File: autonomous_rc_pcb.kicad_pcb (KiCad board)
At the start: 6 copper layers, 91.1 x 143.4 mm, 231 parts, among them J9 Micro_SD_Card, P1 USB_A_Vertical, P2 HDMI_PAUL, P7 USB_A_Vertical, U1 MCP1603L, U10 ECMF04-4HSM10, U11 CM1624, U12 ECMF04-4HSM10, U13 USB2514Bi, U14 LAN9514/LAN9514i, U15 Wurth_Magnetics_749010012A, U16 AP3512E, U2 MCP16311/2, U3 LM2576S-12/NOPB, U4 Autopilot_module, U5 ESD-8040, U6 CC2520, U7 CC2592, U8 CC112X, X1 32Mhz, X2 32MHZ, X3 XRCGB24M000F2P00R0, X4 XRCGB25M000F2P00R0

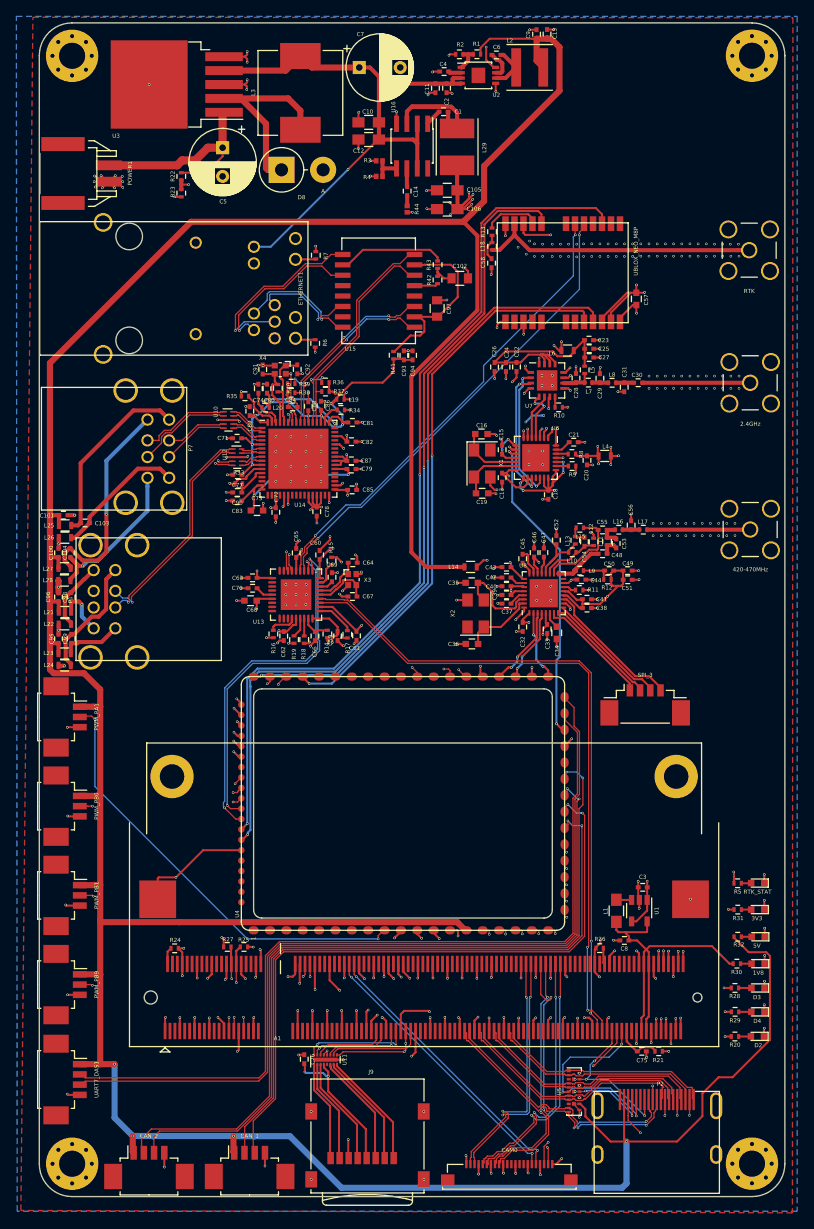
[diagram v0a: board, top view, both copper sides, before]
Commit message: tuned rf
added u.fl connectors to tune line 
moved some lines under rf components
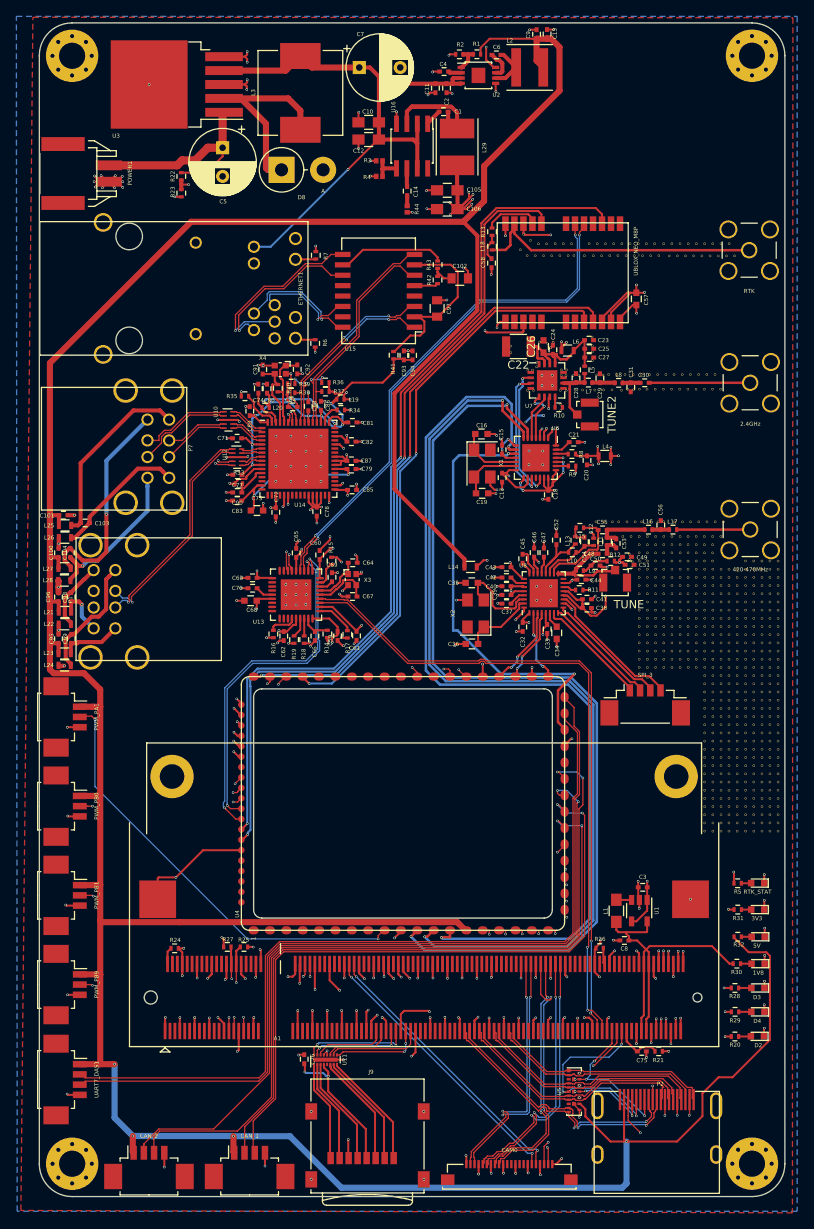
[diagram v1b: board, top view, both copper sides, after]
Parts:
- added REF**: VIA-0.3mm, Don-VIA:VIA-0.3mm, F.Cu at (154.3, 122.7)
- added REF**: VIA-0.3mm, Don-VIA:VIA-0.3mm, F.Cu at (153.3, 126.7)
- added REF**: VIA-0.3mm, Don-VIA:VIA-0.3mm, F.Cu at (155.4, 115.7)
- added REF**: VIA-0.3mm, Don-VIA:VIA-0.3mm, F.Cu at (156.4, 115.7)
- added REF**: VIA-0.3mm, Don-VIA:VIA-0.3mm, F.Cu at (156.4, 116.7)
- added REF**: VIA-0.3mm, Don-VIA:VIA-0.3mm, F.Cu at (156.4, 114.7)
- added REF**: VIA-0.3mm, Don-VIA:VIA-0.3mm, F.Cu at (158.3, 117.7)
- added REF**: VIA-0.3mm, Don-VIA:VIA-0.3mm, F.Cu at (159.3, 117.7)
- added REF**: VIA-0.3mm, Don-VIA:VIA-0.3mm, F.Cu at (159.3, 119.7)
- added REF**: VIA-0.3mm, Don-VIA:VIA-0.3mm, F.Cu at (158.3, 119.7)
- added REF**: VIA-0.3mm, Don-VIA:VIA-0.3mm, F.Cu at (158.3, 118.7)
- added REF**: VIA-0.3mm, Don-VIA:VIA-0.3mm, F.Cu at (159.3, 118.7)
- added REF**: VIA-0.3mm, Don-VIA:VIA-0.3mm, F.Cu at (152.4, 125.7)
- added REF**: VIA-0.3mm, Don-VIA:VIA-0.3mm, F.Cu at (154.3, 114.7)
- added REF**: VIA-0.3mm, Don-VIA:VIA-0.3mm, F.Cu at (154.3, 115.7)
- added REF**: VIA-0.3mm, Don-VIA:VIA-0.3mm, F.Cu at (154.3, 116.7)
- added REF**: VIA-0.3mm, Don-VIA:VIA-0.3mm, F.Cu at (155.4, 114.7)
- added REF**: VIA-0.3mm, Don-VIA:VIA-0.3mm, F.Cu at (154.3, 118.7)
- added REF**: VIA-0.3mm, Don-VIA:VIA-0.3mm, F.Cu at (154.3, 119.7)
- added REF**: VIA-0.3mm, Don-VIA:VIA-0.3mm, F.Cu at (155.4, 119.7)
- added REF**: VIA-0.3mm, Don-VIA:VIA-0.3mm, F.Cu at (155.4, 117.7)
- added REF**: VIA-0.3mm, Don-VIA:VIA-0.3mm, F.Cu at (155.4, 118.7)
- added REF**: VIA-0.3mm, Don-VIA:VIA-0.3mm, F.Cu at (154.3, 117.7)
- added REF**: VIA-0.3mm, Don-VIA:VIA-0.3mm, F.Cu at (150.4, 125.7)
- added REF**: VIA-0.3mm, Don-VIA:VIA-0.3mm, F.Cu at (157.4, 115.7)
- added REF**: VIA-0.3mm, Don-VIA:VIA-0.3mm, F.Cu at (158.3, 114.7)
- added REF**: VIA-0.3mm, Don-VIA:VIA-0.3mm, F.Cu at (157.4, 114.7)
- added REF**: VIA-0.3mm, Don-VIA:VIA-0.3mm, F.Cu at (159.3, 114.7)
- added REF**: VIA-0.3mm, Don-VIA:VIA-0.3mm, F.Cu at (158.3, 115.7)
- added REF**: VIA-0.3mm, Don-VIA:VIA-0.3mm, F.Cu at (157.4, 117.7)
- added REF**: VIA-0.3mm, Don-VIA:VIA-0.3mm, F.Cu at (156.4, 118.7)
- added REF**: VIA-0.3mm, Don-VIA:VIA-0.3mm, F.Cu at (157.4, 118.7)
- added REF**: VIA-0.3mm, Don-VIA:VIA-0.3mm, F.Cu at (157.4, 119.7)
- added REF**: VIA-0.3mm, Don-VIA:VIA-0.3mm, F.Cu at (156.4, 119.7)
- added REF**: VIA-0.3mm, Don-VIA:VIA-0.3mm, F.Cu at (151.4, 125.7)
- added REF**: VIA-0.3mm, Don-VIA:VIA-0.3mm, F.Cu at (156.4, 117.7)
- added REF**: VIA-0.3mm, Don-VIA:VIA-0.3mm, F.Cu at (152.4, 108.7)
- added REF**: VIA-0.3mm, Don-VIA:VIA-0.3mm, F.Cu at (153.3, 108.7)
- added REF**: VIA-0.3mm, Don-VIA:VIA-0.3mm, F.Cu at (152.4, 109.7)
- added REF**: VIA-0.3mm, Don-VIA:VIA-0.3mm, F.Cu at (154.3, 108.7)
- added REF**: VIA-0.3mm, Don-VIA:VIA-0.3mm, F.Cu at (153.3, 109.7)
- added REF**: VIA-0.3mm, Don-VIA:VIA-0.3mm, F.Cu at (154.3, 109.7)
- added REF**: VIA-0.3mm, Don-VIA:VIA-0.3mm, F.Cu at (154.3, 113.7)
- added REF**: VIA-0.3mm, Don-VIA:VIA-0.3mm, F.Cu at (153.3, 113.7)
- added REF**: VIA-0.3mm, Don-VIA:VIA-0.3mm, F.Cu at (153.3, 112.7)
- added REF**: VIA-0.3mm, Don-VIA:VIA-0.3mm, F.Cu at (151.4, 126.7)
- added REF**: VIA-0.3mm, Don-VIA:VIA-0.3mm, F.Cu at (152.4, 113.7)
- added REF**: VIA-0.3mm, Don-VIA:VIA-0.3mm, F.Cu at (154.3, 111.7)
- added REF**: VIA-0.3mm, Don-VIA:VIA-0.3mm, F.Cu at (154.3, 112.7)
- added REF**: VIA-0.3mm, Don-VIA:VIA-0.3mm, F.Cu at (152.4, 112.7)
- added REF**: VIA-0.3mm, Don-VIA:VIA-0.3mm, F.Cu at (154.3, 110.7)
- added REF**: VIA-0.3mm, Don-VIA:VIA-0.3mm, F.Cu at (151.4, 113.7)
- added REF**: VIA-0.3mm, Don-VIA:VIA-0.3mm, F.Cu at (150.4, 113.7)
- added REF**: VIA-0.3mm, Don-VIA:VIA-0.3mm, F.Cu at (150.4, 112.7)
- added REF**: VIA-0.3mm, Don-VIA:VIA-0.3mm, F.Cu at (151.4, 112.7)
- added REF**: VIA-0.3mm, Don-VIA:VIA-0.3mm, F.Cu at (150.4, 111.7)
- added REF**: VIA-0.3mm, Don-VIA:VIA-0.3mm, F.Cu at (150.4, 126.7)
- added REF**: VIA-0.3mm, Don-VIA:VIA-0.3mm, F.Cu at (150.4, 110.7)
- added REF**: VIA-0.3mm, Don-VIA:VIA-0.3mm, F.Cu at (151.4, 111.7)
- added REF**: VIA-0.3mm, Don-VIA:VIA-0.3mm, F.Cu at (151.4, 110.7)
- added REF**: VIA-0.3mm, Don-VIA:VIA-0.3mm, F.Cu at (151.4, 107.7)
- added REF**: VIA-0.3mm, Don-VIA:VIA-0.3mm, F.Cu at (150.4, 107.7)
- added REF**: VIA-0.3mm, Don-VIA:VIA-0.3mm, F.Cu at (153.3, 107.7)
- added REF**: VIA-0.3mm, Don-VIA:VIA-0.3mm, F.Cu at (152.4, 107.7)
- added REF**: VIA-0.3mm, Don-VIA:VIA-0.3mm, F.Cu at (154.3, 107.7)
- added REF**: VIA-0.3mm, Don-VIA:VIA-0.3mm, F.Cu at (157.4, 113.7)
- added REF**: VIA-0.3mm, Don-VIA:VIA-0.3mm, F.Cu at (155.4, 111.7)
- added REF**: VIA-0.3mm, Don-VIA:VIA-0.3mm, F.Cu at (150.4, 123.7)
- added REF**: VIA-0.3mm, Don-VIA:VIA-0.3mm, F.Cu at (155.4, 112.7)
- added REF**: VIA-0.3mm, Don-VIA:VIA-0.3mm, F.Cu at (155.4, 113.7)
- added REF**: VIA-0.3mm, Don-VIA:VIA-0.3mm, F.Cu at (156.4, 113.7)
- added REF**: VIA-0.3mm, Don-VIA:VIA-0.3mm, F.Cu at (159.3, 113.7)
- added REF**: VIA-0.3mm, Don-VIA:VIA-0.3mm, F.Cu at (158.3, 111.7)
- added REF**: VIA-0.3mm, Don-VIA:VIA-0.3mm, F.Cu at (159.3, 112.7)
- added REF**: VIA-0.3mm, Don-VIA:VIA-0.3mm, F.Cu at (159.3, 111.7)
- added REF**: VIA-0.3mm, Don-VIA:VIA-0.3mm, F.Cu at (158.3, 112.7)
- added REF**: VIA-0.3mm, Don-VIA:VIA-0.3mm, F.Cu at (158.3, 113.7)
- added REF**: VIA-0.3mm, Don-VIA:VIA-0.3mm, F.Cu at (157.4, 112.7)
- added REF**: VIA-0.3mm, Don-VIA:VIA-0.3mm, F.Cu at (150.4, 122.7)
- added REF**: VIA-0.3mm, Don-VIA:VIA-0.3mm, F.Cu at (156.4, 111.7)
- added REF**: VIA-0.3mm, Don-VIA:VIA-0.3mm, F.Cu at (157.4, 111.7)
- added REF**: VIA-0.3mm, Don-VIA:VIA-0.3mm, F.Cu at (156.4, 112.7)
- added REF**: VIA-0.3mm, Don-VIA:VIA-0.3mm, F.Cu at (155.4, 109.7)
- added REF**: VIA-0.3mm, Don-VIA:VIA-0.3mm, F.Cu at (156.4, 110.7)
- added REF**: VIA-0.3mm, Don-VIA:VIA-0.3mm, F.Cu at (155.4, 110.7)
- added REF**: VIA-0.3mm, Don-VIA:VIA-0.3mm, F.Cu at (156.4, 109.7)
- added REF**: VIA-0.3mm, Don-VIA:VIA-0.3mm, F.Cu at (159.3, 109.7)
- added REF**: VIA-0.3mm, Don-VIA:VIA-0.3mm, F.Cu at (158.3, 109.7)
- added REF**: VIA-0.3mm, Don-VIA:VIA-0.3mm, F.Cu at (157.4, 109.7)
- added REF**: VIA-0.3mm, Don-VIA:VIA-0.3mm, F.Cu at (151.4, 123.7)
- added REF**: VIA-0.3mm, Don-VIA:VIA-0.3mm, F.Cu at (158.3, 110.7)
- added REF**: VIA-0.3mm, Don-VIA:VIA-0.3mm, F.Cu at (159.3, 110.7)
- added REF**: VIA-0.3mm, Don-VIA:VIA-0.3mm, F.Cu at (157.4, 110.7)
- added REF**: VIA-0.3mm, Don-VIA:VIA-0.3mm, F.Cu at (156.4, 107.7)
- added REF**: VIA-0.3mm, Don-VIA:VIA-0.3mm, F.Cu at (155.4, 108.7)
- added REF**: VIA-0.3mm, Don-VIA:VIA-0.3mm, F.Cu at (155.4, 107.7)
- added REF**: VIA-0.3mm, Don-VIA:VIA-0.3mm, F.Cu at (156.4, 108.7)
- added REF**: VIA-0.3mm, Don-VIA:VIA-0.3mm, F.Cu at (159.3, 107.7)
- added REF**: VIA-0.3mm, Don-VIA:VIA-0.3mm, F.Cu at (158.3, 108.7)
- added REF**: VIA-0.3mm, Don-VIA:VIA-0.3mm, F.Cu at (157.4, 107.7)
- added REF**: VIA-0.3mm, Don-VIA:VIA-0.3mm, F.Cu at (151.4, 122.7)
- added REF**: VIA-0.3mm, Don-VIA:VIA-0.3mm, F.Cu at (158.3, 107.7)
- added REF**: VIA-0.3mm, Don-VIA:VIA-0.3mm, F.Cu at (159.3, 108.7)
- added REF**: VIA-0.3mm, Don-VIA:VIA-0.3mm, F.Cu at (157.4, 108.7)
- added REF**: VIA-0.3mm, Don-VIA:VIA-0.3mm, F.Cu at (152.4, 110.7)
- added REF**: VIA-0.3mm, Don-VIA:VIA-0.3mm, F.Cu at (153.3, 111.7)
- added REF**: VIA-0.3mm, Don-VIA:VIA-0.3mm, F.Cu at (152.4, 111.7)
- added REF**: VIA-0.3mm, Don-VIA:VIA-0.3mm, F.Cu at (153.3, 110.7)
- added REF**: VIA-0.3mm, Don-VIA:VIA-0.3mm, F.Cu at (151.4, 108.7)
- added REF**: VIA-0.3mm, Don-VIA:VIA-0.3mm, F.Cu at (151.4, 109.7)
- added REF**: VIA-0.3mm, Don-VIA:VIA-0.3mm, F.Cu at (150.4, 109.7)
- added REF**: VIA-0.3mm, Don-VIA:VIA-0.3mm, F.Cu at (154.3, 121.7)
- added REF**: VIA-0.3mm, Don-VIA:VIA-0.3mm, F.Cu at (150.4, 124.7)
- added REF**: VIA-0.3mm, Don-VIA:VIA-0.3mm, F.Cu at (150.4, 108.7)
- added REF**: VIA-0.3mm, Don-VIA:VIA-0.3mm, F.Cu at (142.4, 102.7)
- added REF**: VIA-0.3mm, Don-VIA:VIA-0.3mm, F.Cu at (143.4, 102.7)
- added REF**: VIA-0.3mm, Don-VIA:VIA-0.3mm, F.Cu at (144.4, 102.7)
- added REF**: VIA-0.3mm, Don-VIA:VIA-0.3mm, F.Cu at (145.4, 103.7)
- added REF**: VIA-0.3mm, Don-VIA:VIA-0.3mm, F.Cu at (145.4, 102.7)
- added REF**: VIA-0.3mm, Don-VIA:VIA-0.3mm, F.Cu at (144.4, 103.7)
- added REF**: VIA-0.3mm, Don-VIA:VIA-0.3mm, F.Cu at (143.4, 103.7)
- added REF**: VIA-0.3mm, Don-VIA:VIA-0.3mm, F.Cu at (142.4, 104.7)
- added REF**: VIA-0.3mm, Don-VIA:VIA-0.3mm, F.Cu at (143.4, 104.7)
- added REF**: VIA-0.3mm, Don-VIA:VIA-0.3mm, F.Cu at (151.4, 124.7)
- added REF**: VIA-0.3mm, Don-VIA:VIA-0.3mm, F.Cu at (143.4, 105.7)
- added REF**: VIA-0.3mm, Don-VIA:VIA-0.3mm, F.Cu at (143.4, 106.7)
- added REF**: VIA-0.3mm, Don-VIA:VIA-0.3mm, F.Cu at (142.4, 106.7)
- added REF**: VIA-0.3mm, Don-VIA:VIA-0.3mm, F.Cu at (142.4, 103.7)
- added REF**: VIA-0.3mm, Don-VIA:VIA-0.3mm, F.Cu at (142.4, 105.7)
- added REF**: VIA-0.3mm, Don-VIA:VIA-0.3mm, F.Cu at (148.3, 104.7)
- added REF**: VIA-0.3mm, Don-VIA:VIA-0.3mm, F.Cu at (149.3, 103.7)
- added REF**: VIA-0.3mm, Don-VIA:VIA-0.3mm, F.Cu at (148.3, 103.7)
- added REF**: VIA-0.3mm, Don-VIA:VIA-0.3mm, F.Cu at (147.4, 103.7)
- added REF**: VIA-0.3mm, Don-VIA:VIA-0.3mm, F.Cu at (146.4, 103.7)
- added REF**: VIA-0.3mm, Don-VIA:VIA-0.3mm, F.Cu at (154.3, 124.7)
- added REF**: VIA-0.3mm, Don-VIA:VIA-0.3mm, F.Cu at (147.4, 104.7)
- added REF**: VIA-0.3mm, Don-VIA:VIA-0.3mm, F.Cu at (146.4, 104.7)
- added REF**: VIA-0.3mm, Don-VIA:VIA-0.3mm, F.Cu at (147.4, 105.7)
- added REF**: VIA-0.3mm, Don-VIA:VIA-0.3mm, F.Cu at (146.4, 105.7)
- added REF**: VIA-0.3mm, Don-VIA:VIA-0.3mm, F.Cu at (144.4, 106.7)
- added REF**: VIA-0.3mm, Don-VIA:VIA-0.3mm, F.Cu at (144.4, 105.7)
- added REF**: VIA-0.3mm, Don-VIA:VIA-0.3mm, F.Cu at (145.4, 105.7)
- added REF**: VIA-0.3mm, Don-VIA:VIA-0.3mm, F.Cu at (145.4, 106.7)
- added REF**: VIA-0.3mm, Don-VIA:VIA-0.3mm, F.Cu at (146.4, 106.7)
- added REF**: VIA-0.3mm, Don-VIA:VIA-0.3mm, F.Cu at (145.4, 104.7)
- added REF**: VIA-0.3mm, Don-VIA:VIA-0.3mm, F.Cu at (153.3, 123.7)
- added REF**: VIA-0.3mm, Don-VIA:VIA-0.3mm, F.Cu at (144.4, 104.7)
- added REF**: VIA-0.3mm, Don-VIA:VIA-0.3mm, F.Cu at (147.4, 106.7)
- added REF**: VIA-0.3mm, Don-VIA:VIA-0.3mm, F.Cu at (149.3, 105.7)
- added REF**: VIA-0.3mm, Don-VIA:VIA-0.3mm, F.Cu at (149.3, 106.7)
- added REF**: VIA-0.3mm, Don-VIA:VIA-0.3mm, F.Cu at (148.4, 105.7)
- added REF**: VIA-0.3mm, Don-VIA:VIA-0.3mm, F.Cu at (148.4, 106.7)
- added REF**: VIA-0.3mm, Don-VIA:VIA-0.3mm, F.Cu at (149.3, 104.7)
- added REF**: VIA-0.3mm, Don-VIA:VIA-0.3mm, F.Cu at (146.4, 102.7)
- added REF**: VIA-0.3mm, Don-VIA:VIA-0.3mm, F.Cu at (147.4, 102.7)
- added REF**: VIA-0.3mm, Don-VIA:VIA-0.3mm, F.Cu at (148.3, 101.7)
- added REF**: VIA-0.3mm, Don-VIA:VIA-0.3mm, F.Cu at (153.3, 125.7)
- added REF**: VIA-0.3mm, Don-VIA:VIA-0.3mm, F.Cu at (148.3, 102.7)
- added REF**: VIA-0.3mm, Don-VIA:VIA-0.3mm, F.Cu at (149.3, 101.7)
- added REF**: VIA-0.3mm, Don-VIA:VIA-0.3mm, F.Cu at (149.3, 102.7)
- added REF**: VIA-0.3mm, Don-VIA:VIA-0.3mm, F.Cu at (159.3, 106.7)
- added REF**: VIA-0.3mm, Don-VIA:VIA-0.3mm, F.Cu at (158.3, 106.7)
- added REF**: VIA-0.3mm, Don-VIA:VIA-0.3mm, F.Cu at (158.3, 105.7)
- added REF**: VIA-0.3mm, Don-VIA:VIA-0.3mm, F.Cu at (159.3, 105.7)
- added REF**: VIA-0.3mm, Don-VIA:VIA-0.3mm, F.Cu at (159.3, 104.7)
- added REF**: VIA-0.3mm, Don-VIA:VIA-0.3mm, F.Cu at (157.4, 106.7)
- added REF**: VIA-0.3mm, Don-VIA:VIA-0.3mm, F.Cu at (156.4, 106.7)
- added REF**: VIA-0.3mm, Don-VIA:VIA-0.3mm, F.Cu at (153.3, 124.7)
- added REF**: VIA-0.3mm, Don-VIA:VIA-0.3mm, F.Cu at (155.4, 105.7)
- added REF**: VIA-0.3mm, Don-VIA:VIA-0.3mm, F.Cu at (155.4, 106.7)
- added REF**: VIA-0.3mm, Don-VIA:VIA-0.3mm, F.Cu at (158.3, 104.7)
- added REF**: VIA-0.3mm, Don-VIA:VIA-0.3mm, F.Cu at (156.4, 105.7)
- added REF**: VIA-0.3mm, Don-VIA:VIA-0.3mm, F.Cu at (156.4, 104.7)
- added REF**: VIA-0.3mm, Don-VIA:VIA-0.3mm, F.Cu at (157.4, 105.7)
- added REF**: VIA-0.3mm, Don-VIA:VIA-0.3mm, F.Cu at (157.4, 104.7)
- added REF**: VIA-0.3mm, Don-VIA:VIA-0.3mm, F.Cu at (156.4, 101.7)
- added REF**: VIA-0.3mm, Don-VIA:VIA-0.3mm, F.Cu at (155.4, 101.7)
- added REF**: VIA-0.3mm, Don-VIA:VIA-0.3mm, F.Cu at (158.3, 101.7)
- added REF**: VIA-0.3mm, Don-VIA:VIA-0.3mm, F.Cu at (152.4, 123.7)
- added REF**: VIA-0.3mm, Don-VIA:VIA-0.3mm, F.Cu at (157.4, 101.7)
- added REF**: VIA-0.3mm, Don-VIA:VIA-0.3mm, F.Cu at (159.3, 101.7)
- added REF**: VIA-0.3mm, Don-VIA:VIA-0.3mm, F.Cu at (155.4, 104.7)
- added REF**: VIA-0.3mm, Don-VIA:VIA-0.3mm, F.Cu at (155.4, 103.7)
- added REF**: VIA-0.3mm, Don-VIA:VIA-0.3mm, F.Cu at (156.4, 102.7)
- added REF**: VIA-0.3mm, Don-VIA:VIA-0.3mm, F.Cu at (155.4, 102.7)
- added REF**: VIA-0.3mm, Don-VIA:VIA-0.3mm, F.Cu at (156.4, 103.7)
- added REF**: VIA-0.3mm, Don-VIA:VIA-0.3mm, F.Cu at (158.3, 103.7)
- added REF**: VIA-0.3mm, Don-VIA:VIA-0.3mm, F.Cu at (158.3, 102.7)
- added REF**: VIA-0.3mm, Don-VIA:VIA-0.3mm, F.Cu at (157.4, 103.7)
- added REF**: VIA-0.3mm, Don-VIA:VIA-0.3mm, F.Cu at (154.3, 123.7)
- added REF**: VIA-0.3mm, Don-VIA:VIA-0.3mm, F.Cu at (157.4, 102.7)
- added REF**: VIA-0.3mm, Don-VIA:VIA-0.3mm, F.Cu at (159.3, 102.7)
- added REF**: VIA-0.3mm, Don-VIA:VIA-0.3mm, F.Cu at (159.3, 103.7)
- added REF**: VIA-0.3mm, Don-VIA:VIA-0.3mm, F.Cu at (152.4, 104.7)
- added REF**: VIA-0.3mm, Don-VIA:VIA-0.3mm, F.Cu at (152.4, 103.7)
- added REF**: VIA-0.3mm, Don-VIA:VIA-0.3mm, F.Cu at (153.3, 103.7)
- added REF**: VIA-0.3mm, Don-VIA:VIA-0.3mm, F.Cu at (154.3, 104.7)
- added REF**: VIA-0.3mm, Don-VIA:VIA-0.3mm, F.Cu at (154.3, 102.7)
- added REF**: VIA-0.3mm, Don-VIA:VIA-0.3mm, F.Cu at (154.3, 103.7)
- added REF**: VIA-0.3mm, Don-VIA:VIA-0.3mm, F.Cu at (153.3, 104.7)
- added REF**: VIA-0.3mm, Don-VIA:VIA-0.3mm, F.Cu at (152.4, 124.7)
- added REF**: VIA-0.3mm, Don-VIA:VIA-0.3mm, F.Cu at (150.4, 101.7)
- added REF**: VIA-0.3mm, Don-VIA:VIA-0.3mm, F.Cu at (151.4, 102.7)
- added REF**: VIA-0.3mm, Don-VIA:VIA-0.3mm, F.Cu at (150.4, 103.7)
- added REF**: VIA-0.3mm, Don-VIA:VIA-0.3mm, F.Cu at (150.4, 102.7)
- added REF**: VIA-0.3mm, Don-VIA:VIA-0.3mm, F.Cu at (151.4, 103.7)
- added REF**: VIA-0.3mm, Don-VIA:VIA-0.3mm, F.Cu at (151.4, 101.7)
- added REF**: VIA-0.3mm, Don-VIA:VIA-0.3mm, F.Cu at (153.3, 101.7)
- added REF**: VIA-0.3mm, Don-VIA:VIA-0.3mm, F.Cu at (152.4, 102.7)
- added REF**: VIA-0.3mm, Don-VIA:VIA-0.3mm, F.Cu at (154.3, 101.7)
- added REF**: VIA-0.3mm, Don-VIA:VIA-0.3mm, F.Cu at (152.4, 101.7)
- added REF**: VIA-0.3mm, Don-VIA:VIA-0.3mm, F.Cu at (153.3, 120.7)
- added REF**: VIA-0.3mm, Don-VIA:VIA-0.3mm, F.Cu at (153.3, 102.7)
- added REF**: VIA-0.3mm, Don-VIA:VIA-0.3mm, F.Cu at (150.4, 104.7)
- added REF**: VIA-0.3mm, Don-VIA:VIA-0.3mm, F.Cu at (150.4, 106.7)
- added REF**: VIA-0.3mm, Don-VIA:VIA-0.3mm, F.Cu at (151.4, 105.7)
- added REF**: VIA-0.3mm, Don-VIA:VIA-0.3mm, F.Cu at (151.4, 104.7)
- added REF**: VIA-0.3mm, Don-VIA:VIA-0.3mm, F.Cu at (150.4, 105.7)
- added REF**: VIA-0.3mm, Don-VIA:VIA-0.3mm, F.Cu at (151.4, 106.7)
- added REF**: VIA-0.3mm, Don-VIA:VIA-0.3mm, F.Cu at (154.3, 106.7)
- added REF**: VIA-0.3mm, Don-VIA:VIA-0.3mm, F.Cu at (154.3, 105.7)
- added REF**: VIA-0.3mm, Don-VIA:VIA-0.3mm, F.Cu at (153.3, 105.7)
- added REF**: VIA-0.3mm, Don-VIA:VIA-0.3mm, F.Cu at (153.3, 122.7)
- added REF**: VIA-0.3mm, Don-VIA:VIA-0.3mm, F.Cu at (152.4, 120.7)
- added REF**: VIA-0.3mm, Don-VIA:VIA-0.3mm, F.Cu at (153.3, 106.7)
- added REF**: VIA-0.3mm, Don-VIA:VIA-0.3mm, F.Cu at (152.4, 106.7)
- added REF**: VIA-0.3mm, Don-VIA:VIA-0.3mm, F.Cu at (152.4, 105.7)
- added REF**: VIA-0.3mm, Don-VIA:VIA-0.3mm, F.Cu at (147.4, 101.7)
- added REF**: VIA-0.3mm, Don-VIA:VIA-0.3mm, F.Cu at (146.4, 101.7)
- added REF**: VIA-0.3mm, Don-VIA:VIA-0.3mm, F.Cu at (144.4, 101.7)
- added REF**: VIA-0.3mm, Don-VIA:VIA-0.3mm, F.Cu at (145.4, 101.7)
- added REF**: VIA-0.3mm, Don-VIA:VIA-0.3mm, F.Cu at (143.4, 101.7)
- added REF**: VIA-0.3mm, Don-VIA:VIA-0.3mm, F.Cu at (142.4, 101.7)
- added REF**: VIA-0.3mm, Don-VIA:VIA-0.3mm, F.Cu at (144.4, 97.7)
- added REF**: VIA-0.3mm, Don-VIA:VIA-0.3mm, F.Cu at (154.3, 120.7)
- added REF**: VIA-0.3mm, Don-VIA:VIA-0.3mm, F.Cu at (142.4, 99.7)
- added REF**: VIA-0.3mm, Don-VIA:VIA-0.3mm, F.Cu at (142.4, 100.7)
- added REF**: VIA-0.3mm, Don-VIA:VIA-0.3mm, F.Cu at (143.4, 100.7)
- added REF**: VIA-0.3mm, Don-VIA:VIA-0.3mm, F.Cu at (143.4, 99.7)
- added REF**: VIA-0.3mm, Don-VIA:VIA-0.3mm, F.Cu at (144.4, 98.7)
- added REF**: VIA-0.3mm, Don-VIA:VIA-0.3mm, F.Cu at (143.4, 98.7)
- added REF**: VIA-0.3mm, Don-VIA:VIA-0.3mm, F.Cu at (144.4, 99.7)
- added REF**: VIA-0.3mm, Don-VIA:VIA-0.3mm, F.Cu at (142.4, 98.7)
- added REF**: VIA-0.3mm, Don-VIA:VIA-0.3mm, F.Cu at (143.4, 96.7)
- added REF**: VIA-0.3mm, Don-VIA:VIA-0.3mm, F.Cu at (142.4, 97.7)
- added REF**: VIA-0.3mm, Don-VIA:VIA-0.3mm, F.Cu at (150.4, 121.7)
- added REF**: VIA-0.3mm, Don-VIA:VIA-0.3mm, F.Cu at (142.4, 96.7)
- added REF**: VIA-0.3mm, Don-VIA:VIA-0.3mm, F.Cu at (143.4, 97.7)
- added REF**: VIA-0.3mm, Don-VIA:VIA-0.3mm, F.Cu at (144.4, 100.7)
- added REF**: VIA-0.3mm, Don-VIA:VIA-0.3mm, F.Cu at (144.4, 96.7)
- added REF**: VIA-0.3mm, Don-VIA:VIA-0.3mm, F.Cu at (144.4, 95.7)
- added REF**: VIA-0.3mm, Don-VIA:VIA-0.3mm, F.Cu at (144.4, 93.7)
- added REF**: VIA-0.3mm, Don-VIA:VIA-0.3mm, F.Cu at (144.4, 94.7)
- added REF**: VIA-0.3mm, Don-VIA:VIA-0.3mm, F.Cu at (144.4, 92.7)
- added REF**: VIA-0.3mm, Don-VIA:VIA-0.3mm, F.Cu at (144.4, 91.7)
- added REF**: VIA-0.3mm, Don-VIA:VIA-0.3mm, F.Cu at (143.4, 93.7)
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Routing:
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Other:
- rule pad_to_mask_clearance: 0.2 -> 0.1

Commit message: stitched pcb, tuned rf
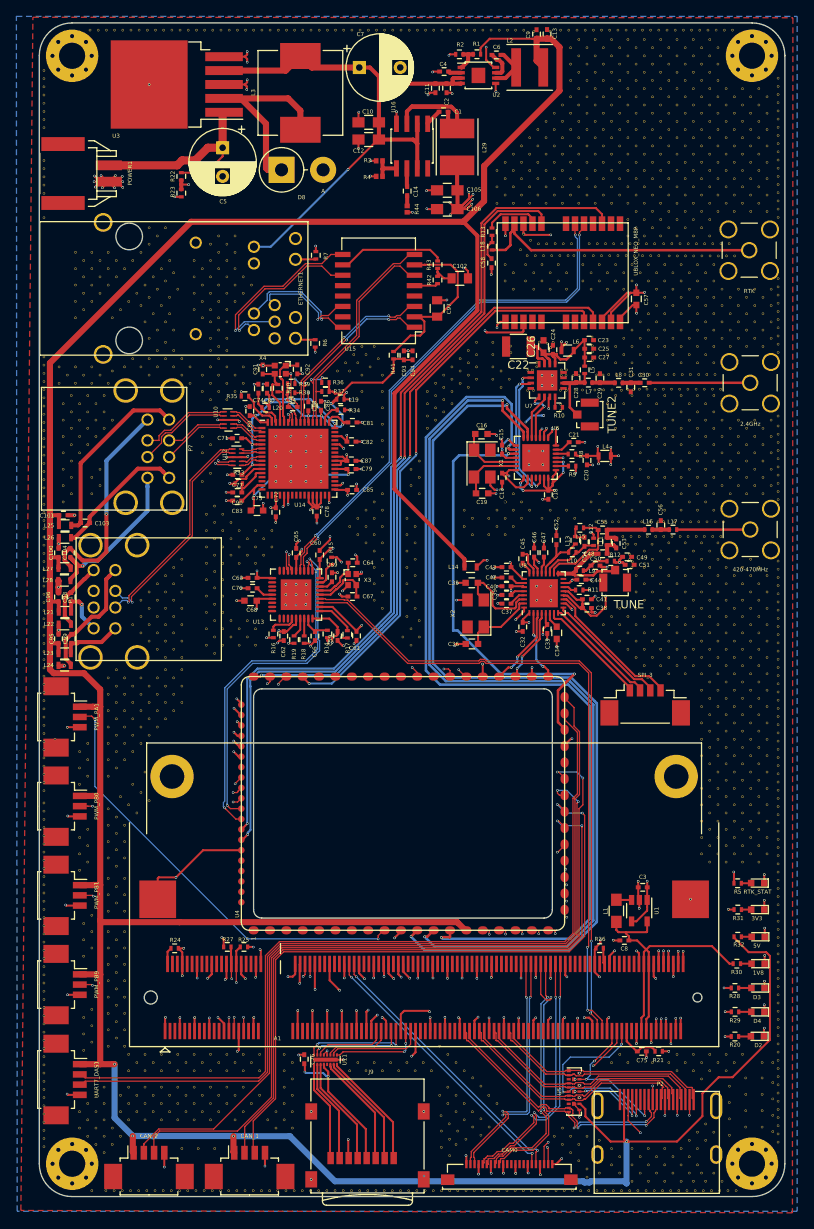
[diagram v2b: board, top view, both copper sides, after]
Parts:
- removed the REF** at (154.3, 122.7)
- removed the REF** at (153.3, 126.7)
- removed the REF** at (155.4, 115.7)
- removed the REF** at (156.4, 115.7)
- removed the REF** at (156.4, 116.7)
- removed the REF** at (156.4, 114.7)
- removed the REF** at (158.3, 117.7)
- removed the REF** at (158.3, 119.7)
- removed the REF** at (158.3, 118.7)
- removed the REF** at (152.4, 125.7)
- removed the REF** at (154.3, 114.7)
- removed the REF** at (154.3, 115.7)
- removed the REF** at (154.3, 116.7)
- removed the REF** at (155.4, 114.7)
- removed the REF** at (154.3, 118.7)
- removed the REF** at (154.3, 119.7)
- removed the REF** at (155.4, 119.7)
- removed the REF** at (155.4, 117.7)
- removed the REF** at (155.4, 118.7)
- removed the REF** at (154.3, 117.7)
- removed the REF** at (150.4, 125.7)
- removed the REF** at (157.4, 115.7)
- removed the REF** at (158.3, 114.7)
- removed the REF** at (157.4, 114.7)
- removed the REF** at (158.3, 115.7)
- removed the REF** at (157.4, 117.7)
- removed the REF** at (156.4, 118.7)
- removed the REF** at (157.4, 118.7)
- removed the REF** at (157.4, 119.7)
- removed the REF** at (156.4, 119.7)
- removed the REF** at (151.4, 125.7)
- removed the REF** at (156.4, 117.7)
- removed the REF** at (152.4, 108.7)
- removed the REF** at (153.3, 108.7)
- removed the REF** at (152.4, 109.7)
- removed the REF** at (154.3, 108.7)
- removed the REF** at (153.3, 109.7)
- removed the REF** at (154.3, 109.7)
- removed the REF** at (154.3, 113.7)
- removed the REF** at (153.3, 113.7)
- removed the REF** at (153.3, 112.7)
- removed the REF** at (151.4, 126.7)
- removed the REF** at (152.4, 113.7)
- removed the REF** at (154.3, 111.7)
- removed the REF** at (154.3, 112.7)
- removed the REF** at (152.4, 112.7)
- removed the REF** at (154.3, 110.7)
- removed the REF** at (151.4, 113.7)
- removed the REF** at (150.4, 113.7)
- removed the REF** at (150.4, 112.7)
- removed the REF** at (151.4, 112.7)
- removed the REF** at (150.4, 111.7)
- removed the REF** at (150.4, 126.7)
- removed the REF** at (150.4, 110.7)
- removed the REF** at (151.4, 111.7)
- removed the REF** at (151.4, 110.7)
- removed the REF** at (151.4, 107.7)
- removed the REF** at (150.4, 107.7)
- removed the REF** at (153.3, 107.7)
- removed the REF** at (152.4, 107.7)
- removed the REF** at (154.3, 107.7)
- removed the REF** at (157.4, 113.7)
- removed the REF** at (155.4, 111.7)
- removed the REF** at (150.4, 123.7)
- removed the REF** at (155.4, 112.7)
- removed the REF** at (155.4, 113.7)
- removed the REF** at (156.4, 113.7)
- removed the REF** at (158.3, 111.7)
- removed the REF** at (158.3, 112.7)
- removed the REF** at (158.3, 113.7)
- removed the REF** at (157.4, 112.7)
- removed the REF** at (150.4, 122.7)
- removed the REF** at (156.4, 111.7)
- removed the REF** at (157.4, 111.7)
- removed the REF** at (156.4, 112.7)
- removed the REF** at (155.4, 109.7)
- removed the REF** at (156.4, 110.7)
- removed the REF** at (155.4, 110.7)
- removed the REF** at (156.4, 109.7)
- removed the REF** at (158.3, 109.7)
- removed the REF** at (157.4, 109.7)
- removed the REF** at (151.4, 123.7)
- removed the REF** at (158.3, 110.7)
- removed the REF** at (157.4, 110.7)
- removed the REF** at (156.4, 107.7)
- removed the REF** at (155.4, 108.7)
- removed the REF** at (155.4, 107.7)
- removed the REF** at (156.4, 108.7)
- removed the REF** at (158.3, 108.7)
- removed the REF** at (157.4, 107.7)
- removed the REF** at (151.4, 122.7)
- removed the REF** at (158.3, 107.7)
- removed the REF** at (157.4, 108.7)
- removed the REF** at (152.4, 110.7)
- removed the REF** at (153.3, 111.7)
- removed the REF** at (152.4, 111.7)
- removed the REF** at (153.3, 110.7)
- removed the REF** at (151.4, 108.7)
- removed the REF** at (151.4, 109.7)
- removed the REF** at (150.4, 109.7)
- removed the REF** at (154.3, 121.7)
- removed the REF** at (150.4, 124.7)
- removed the REF** at (150.4, 108.7)
- removed the REF** at (142.4, 102.7)
- removed the REF** at (143.4, 102.7)
- removed the REF** at (144.4, 102.7)
- removed the REF** at (145.4, 103.7)
- removed the REF** at (145.4, 102.7)
- removed the REF** at (144.4, 103.7)
- removed the REF** at (143.4, 103.7)
- removed the REF** at (142.4, 104.7)
- removed the REF** at (143.4, 104.7)
- removed the REF** at (151.4, 124.7)
- removed the REF** at (143.4, 105.7)
- removed the REF** at (143.4, 106.7)
- removed the REF** at (142.4, 106.7)
- removed the REF** at (142.4, 103.7)
- removed the REF** at (142.4, 105.7)
- removed the REF** at (148.3, 104.7)
- removed the REF** at (149.3, 103.7)
- removed the REF** at (148.3, 103.7)
- removed the REF** at (147.4, 103.7)
- removed the REF** at (146.4, 103.7)
- removed the REF** at (154.3, 124.7)
- removed the REF** at (147.4, 104.7)
- removed the REF** at (146.4, 104.7)
- removed the REF** at (147.4, 105.7)
- removed the REF** at (146.4, 105.7)
- removed the REF** at (144.4, 106.7)
- removed the REF** at (144.4, 105.7)
- removed the REF** at (145.4, 105.7)
- removed the REF** at (145.4, 106.7)
- removed the REF** at (146.4, 106.7)
- removed the REF** at (145.4, 104.7)
- removed the REF** at (153.3, 123.7)
- removed the REF** at (144.4, 104.7)
- removed the REF** at (147.4, 106.7)
- removed the REF** at (149.3, 105.7)
- removed the REF** at (149.3, 106.7)
- removed the REF** at (148.4, 105.7)
- removed the REF** at (148.4, 106.7)
- removed the REF** at (149.3, 104.7)
- removed the REF** at (146.4, 102.7)
- removed the REF** at (147.4, 102.7)
- removed the REF** at (148.3, 101.7)
- removed the REF** at (153.3, 125.7)
- removed the REF** at (148.3, 102.7)
- removed the REF** at (149.3, 101.7)
- removed the REF** at (149.3, 102.7)
- removed the REF** at (158.3, 106.7)
- removed the REF** at (158.3, 105.7)
- removed the REF** at (157.4, 106.7)
- removed the REF** at (156.4, 106.7)
- removed the REF** at (153.3, 124.7)
- removed the REF** at (155.4, 105.7)
- removed the REF** at (155.4, 106.7)
- removed the REF** at (158.3, 104.7)
- removed the REF** at (156.4, 105.7)
- removed the REF** at (156.4, 104.7)
- removed the REF** at (157.4, 105.7)
- removed the REF** at (157.4, 104.7)
- removed the REF** at (156.4, 101.7)
- removed the REF** at (155.4, 101.7)
- removed the REF** at (158.3, 101.7)
- removed the REF** at (152.4, 123.7)
- removed the REF** at (157.4, 101.7)
- removed the REF** at (155.4, 104.7)
- removed the REF** at (155.4, 103.7)
- removed the REF** at (156.4, 102.7)
- removed the REF** at (155.4, 102.7)
- removed the REF** at (156.4, 103.7)
- removed the REF** at (158.3, 103.7)
- removed the REF** at (158.3, 102.7)
- removed the REF** at (157.4, 103.7)
- removed the REF** at (154.3, 123.7)
- removed the REF** at (157.4, 102.7)
- removed the REF** at (152.4, 104.7)
- removed the REF** at (152.4, 103.7)
- removed the REF** at (153.3, 103.7)
- removed the REF** at (154.3, 104.7)
- removed the REF** at (154.3, 102.7)
- removed the REF** at (154.3, 103.7)
- removed the REF** at (153.3, 104.7)
- removed the REF** at (152.4, 124.7)
- removed the REF** at (150.4, 101.7)
- removed the REF** at (151.4, 102.7)
- removed the REF** at (150.4, 103.7)
- removed the REF** at (150.4, 102.7)
- removed the REF** at (151.4, 103.7)
- removed the REF** at (151.4, 101.7)
- removed the REF** at (153.3, 101.7)
- removed the REF** at (152.4, 102.7)
- removed the REF** at (154.3, 101.7)
- removed the REF** at (152.4, 101.7)
- removed the REF** at (153.3, 120.7)
- removed the REF** at (153.3, 102.7)
- removed the REF** at (150.4, 104.7)
- removed the REF** at (150.4, 106.7)
- removed the REF** at (151.4, 105.7)
- removed the REF** at (151.4, 104.7)
- removed the REF** at (150.4, 105.7)
- removed the REF** at (151.4, 106.7)
- removed the REF** at (154.3, 106.7)
- removed the REF** at (154.3, 105.7)
- removed the REF** at (153.3, 105.7)
- removed the REF** at (153.3, 122.7)
- removed the REF** at (152.4, 120.7)
- removed the REF** at (153.3, 106.7)
- removed the REF** at (152.4, 106.7)
- removed the REF** at (152.4, 105.7)
- removed the REF** at (147.4, 101.7)
- removed the REF** at (146.4, 101.7)
- removed the REF** at (144.4, 101.7)
- removed the REF** at (145.4, 101.7)
- removed the REF** at (143.4, 101.7)
- removed the REF** at (142.4, 101.7)
- removed the REF** at (144.4, 97.7)
- removed the REF** at (154.3, 120.7)
- removed the REF** at (142.4, 99.7)
- removed the REF** at (142.4, 100.7)
- removed the REF** at (143.4, 100.7)
- removed the REF** at (143.4, 99.7)
- removed the REF** at (144.4, 98.7)
- removed the REF** at (143.4, 98.7)
- removed the REF** at (144.4, 99.7)
- removed the REF** at (142.4, 98.7)
- removed the REF** at (143.4, 96.7)
- removed the REF** at (142.4, 97.7)
- removed the REF** at (150.4, 121.7)
- removed the REF** at (142.4, 96.7)
- removed the REF** at (143.4, 97.7)
- removed the REF** at (144.4, 100.7)
- removed the REF** at (144.4, 96.7)
- removed the REF** at (144.4, 95.7)
- removed the REF** at (144.4, 93.7)
- removed the REF** at (144.4, 94.7)
- removed the REF** at (144.4, 92.7)
- removed the REF** at (144.4, 91.7)
- removed the REF** at (143.4, 93.7)
- removed the REF** at (150.4, 120.7)
- removed the REF** at (142.4, 93.7)
- removed the REF** at (142.4, 91.7)
- removed the REF** at (143.4, 92.7)
- removed the REF** at (143.4, 91.7)
- removed the REF** at (142.4, 92.7)
- removed the REF** at (143.4, 95.7)
- removed the REF** at (142.4, 95.7)
- removed the REF** at (142.4, 94.7)
- removed the REF** at (143.4, 94.7)
- removed the REF** at (145.4, 100.7)
- removed the REF** at (151.4, 120.7)
- removed the REF** at (145.4, 99.7)
- removed the REF** at (147.4, 99.7)
- removed the REF** at (146.4, 100.7)
- removed the REF** at (147.4, 100.7)
- removed the REF** at (146.4, 99.7)
- removed the REF** at (149.3, 100.7)
- removed the REF** at (148.4, 100.7)
- removed the REF** at (149.3, 99.7)
- removed the REF** at (148.4, 99.7)
- removed the REF** at (150.3, 93.7)
- removed the REF** at (151.4, 121.7)
- removed the REF** at (150.3, 92.7)
- removed the REF** at (150.3, 91.7)
- removed the REF** at (151.3, 92.7)
- removed the REF** at (151.3, 91.7)
- removed the REF** at (151.3, 93.7)
- removed the REF** at (145.4, 96.7)
- removed the REF** at (146.4, 95.7)
- removed the REF** at (145.4, 95.7)
- removed the REF** at (146.4, 96.7)
- removed the REF** at (145.4, 97.7)
- removed the REF** at (145.4, 98.7)
- removed the REF** at (146.4, 97.7)
- removed the REF** at (146.4, 98.7)
- removed the REF** at (149.3, 98.7)
- removed the REF** at (147.4, 96.7)
- removed the REF** at (148.3, 95.7)
- removed the REF** at (149.3, 96.7)
- removed the REF** at (149.3, 95.7)
- removed the REF** at (147.4, 95.7)
- removed the REF** at (148.3, 96.7)
- removed the REF** at (158.3, 120.7)
- removed the REF** at (148.3, 98.7)
- removed the REF** at (147.4, 97.7)
- removed the REF** at (149.3, 97.7)
- removed the REF** at (148.3, 97.7)
- removed the REF** at (147.4, 98.7)
- removed the REF** at (150.4, 100.7)
- removed the REF** at (153.3, 100.7)
- removed the REF** at (152.4, 100.7)
- removed the REF** at (154.3, 100.7)
- removed the REF** at (153.3, 99.7)
- removed the REF** at (155.4, 120.7)
- removed the REF** at (151.4, 100.7)
- removed the REF** at (153.3, 97.7)
- removed the REF** at (152.4, 97.7)
- removed the REF** at (154.3, 97.7)
- removed the REF** at (153.3, 95.7)
- removed the REF** at (154.3, 96.7)
- removed the REF** at (152.4, 96.7)
- removed the REF** at (153.3, 96.7)
- removed the REF** at (152.4, 95.7)
- removed the REF** at (152.4, 98.7)
- removed the REF** at (156.4, 120.7)
- removed the REF** at (154.3, 98.7)
- removed the REF** at (154.3, 99.7)
- removed the REF** at (153.3, 98.7)
- removed the REF** at (152.4, 99.7)
- removed the REF** at (150.4, 97.7)
- removed the REF** at (150.4, 99.7)
- removed the REF** at (151.4, 97.7)
- removed the REF** at (150.4, 98.7)
- removed the REF** at (151.4, 98.7)
- removed the REF** at (151.4, 99.7)
- removed the REF** at (152.4, 121.7)
- removed the REF** at (157.4, 120.7)
- removed the REF** at (151.4, 96.7)
- removed the REF** at (154.3, 95.7)
- removed the REF** at (153.3, 94.7)
- removed the REF** at (154.3, 94.7)
- removed the REF** at (152.4, 94.7)
- removed the REF** at (150.4, 94.7)
- removed the REF** at (150.4, 96.7)
- removed the REF** at (151.4, 95.7)
- removed the REF** at (150.4, 95.7)
- removed the REF** at (151.4, 94.7)
- removed the REF** at (158.3, 122.7)
- removed the REF** at (158.3, 99.7)
- removed the REF** at (157.4, 99.7)
- removed the REF** at (157.4, 98.7)
- removed the REF** at (158.3, 98.7)
- removed the REF** at (158.3, 97.7)
- removed the REF** at (157.4, 97.7)
- removed the REF** at (156.4, 98.7)
- removed the REF** at (158.3, 121.7)
- removed the REF** at (155.4, 97.7)
- removed the REF** at (156.4, 97.7)
- removed the REF** at (155.4, 98.7)
- removed the REF** at (156.4, 100.7)
- removed the REF** at (158.3, 100.7)
- removed the REF** at (155.4, 100.7)
- removed the REF** at (157.4, 100.7)
- removed the REF** at (156.4, 99.7)
- removed the REF** at (155.4, 99.7)
- removed the REF** at (157.4, 121.7)
- removed the REF** at (158.3, 95.7)
- removed the REF** at (157.4, 95.7)
- removed the REF** at (157.4, 94.7)
- removed the REF** at (158.3, 94.7)
- removed the REF** at (158.3, 93.7)
- removed the REF** at (157.4, 93.7)
- removed the REF** at (156.4, 94.7)
- removed the REF** at (155.4, 93.7)
- removed the REF** at (156.4, 93.7)
- removed the REF** at (155.4, 94.7)
- removed the REF** at (156.4, 96.7)
- removed the REF** at (158.3, 96.7)
- removed the REF** at (155.4, 96.7)
- removed the REF** at (157.4, 96.7)
- removed the REF** at (156.4, 95.7)
- removed the REF** at (155.4, 95.7)
- removed the REF** at (147.4, 94.7)
- removed the REF** at (148.3, 93.7)
- removed the REF** at (149.3, 93.7)
- removed the REF** at (147.4, 93.7)
- removed the REF** at (149.3, 94.7)
- removed the REF** at (148.3, 94.7)
- removed the REF** at (145.4, 94.7)
- removed the REF** at (145.4, 93.7)
- removed the REF** at (146.4, 93.7)
- removed the REF** at (146.4, 94.7)
- removed the REF** at (157.4, 122.7)
- removed the REF** at (147.4, 92.7)
- removed the REF** at (148.3, 92.7)
- removed the REF** at (146.4, 92.7)
- removed the REF** at (149.3, 92.7)
- removed the REF** at (145.4, 92.7)
- removed the REF** at (147.4, 91.7)
- removed the REF** at (148.3, 91.7)
- removed the REF** at (146.4, 91.7)
- removed the REF** at (149.3, 91.7)
- removed the REF** at (145.4, 91.7)
- removed the REF** at (156.4, 124.7)
- removed the REF** at (156.4, 125.7)
- removed the REF** at (155.4, 125.7)
- removed the REF** at (152.4, 122.7)
- removed the REF** at (155.4, 124.7)
- removed the REF** at (155.4, 126.7)
- removed the REF** at (156.4, 126.7)
- removed the REF** at (157.4, 126.7)
- removed the REF** at (158.3, 125.7)
- removed the REF** at (158.3, 126.7)
- removed the REF** at (157.4, 125.7)
- removed the REF** at (155.4, 121.7)
- removed the REF** at (153.3, 121.7)
- removed the REF** at (156.4, 123.7)
- removed the REF** at (156.4, 122.7)
- removed the REF** at (155.4, 122.7)
- removed the REF** at (155.4, 123.7)
- removed the REF** at (156.4, 121.7)
- removed the REF** at (157.4, 124.7)
- removed the REF** at (158.3, 124.7)
- removed the REF** at (157.4, 123.7)
- removed the REF** at (158.3, 123.7)
- removed the REF** at (154.3, 126.7)
- removed the REF** at (151.4, 114.7)
- removed the REF** at (153.3, 114.7)
- removed the REF** at (152.4, 114.7)
- removed the REF** at (153.3, 115.7)
- removed the REF** at (152.4, 115.7)
- removed the REF** at (150.4, 117.7)
- removed the REF** at (151.4, 119.7)
- removed the REF** at (151.4, 118.7)
- removed the REF** at (150.4, 118.7)
- removed the REF** at (152.4, 126.7)
- removed the REF** at (150.4, 119.7)
- removed the REF** at (151.4, 115.7)
- removed the REF** at (151.4, 116.7)
- removed the REF** at (152.4, 116.7)
- removed the REF** at (153.3, 116.7)
- removed the REF** at (151.4, 117.7)
- removed the REF** at (152.4, 118.7)
- removed the REF** at (152.4, 119.7)
- removed the REF** at (152.4, 117.7)
- removed the REF** at (153.3, 119.7)
- removed the REF** at (154.3, 125.7)
- removed the REF** at (153.3, 117.7)
- removed the REF** at (153.3, 118.7)
- removed the REF** at (150.4, 114.7)
- removed the REF** at (150.4, 115.7)
- removed the REF** at (150.4, 116.7)
- removed the REF** at (158.3, 116.7)
- removed the REF** at (157.4, 116.7)
- removed the REF** at (155.4, 116.7)
- added REF**: VIA-0.3mm, Don-VIA:VIA-0.3mm, F.Cu at (127.0, 60.5)
- added REF**: VIA-0.3mm, Don-VIA:VIA-0.3mm, F.Cu at (130.5, 59.5)
- added REF**: VIA-0.3mm, Don-VIA:VIA-0.3mm, F.Cu at (127.0, 89.5)
- added REF**: VIA-0.3mm, Don-VIA:VIA-0.3mm, F.Cu at (94.0, 70.0)
- added REF**: VIA-0.3mm, Don-VIA:VIA-0.3mm, F.Cu at (93.0, 71.0)
- added REF**: VIA-0.3mm, Don-VIA:VIA-0.3mm, F.Cu at (92.0, 70.0)
- added REF**: VIA-0.3mm, Don-VIA:VIA-0.3mm, F.Cu at (90.0, 70.0)
- added REF**: VIA-0.3mm, Don-VIA:VIA-0.3mm, F.Cu at (90.0, 74.0)
- added REF**: VIA-0.3mm, Don-VIA:VIA-0.3mm, F.Cu at (92.0, 72.0)
- added REF**: VIA-0.3mm, Don-VIA:VIA-0.3mm, F.Cu at (91.0, 71.0)
- added REF**: VIA-0.3mm, Don-VIA:VIA-0.3mm, F.Cu at (91.0, 73.0)
- added REF**: VIA-0.3mm, Don-VIA:VIA-0.3mm, F.Cu at (90.0, 72.0)
- added REF**: VIA-0.3mm, Don-VIA:VIA-0.3mm, F.Cu at (89.0, 73.0)
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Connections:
- CAN_1 pad : (no net) -> GND
- CAN_2 pad : (no net) -> GND
- PWM_PA1 pad : (no net) -> GND
- PWM_PB0 pad : (no net) -> GND
- PWM_PB1 pad : (no net) -> GND
- PWM_PB9 pad : (no net) -> GND
- UART7_DAS1 pad : (no net) -> GND
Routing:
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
